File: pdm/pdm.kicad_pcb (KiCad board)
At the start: 2 copper layers, 169.5 x 69 mm, 100 parts, among them J1 Conn_01x05, J2 Conn_01x04_Male, Q1 Q_NPN_BCE, Q10 MMBT3904, Q2 Q_NPN_BCE, Q3 Q_NPN_BCE, Q4 Q_NPN_BCE, Q5 Q_NPN_BCE, Q6 MMBT3904, Q7 MMBT3904, Q8 MMBT3904, Q9 MMBT3904, SW1 SW_Push, U1 AZ1117CH-3_3TRG1, U10 BTS443P, U12 BTS443P, U2 SN65HVD233, U3 STM32F042G6Ux, U4 BTS443P, U6 BTS443P, U8 BTS443P

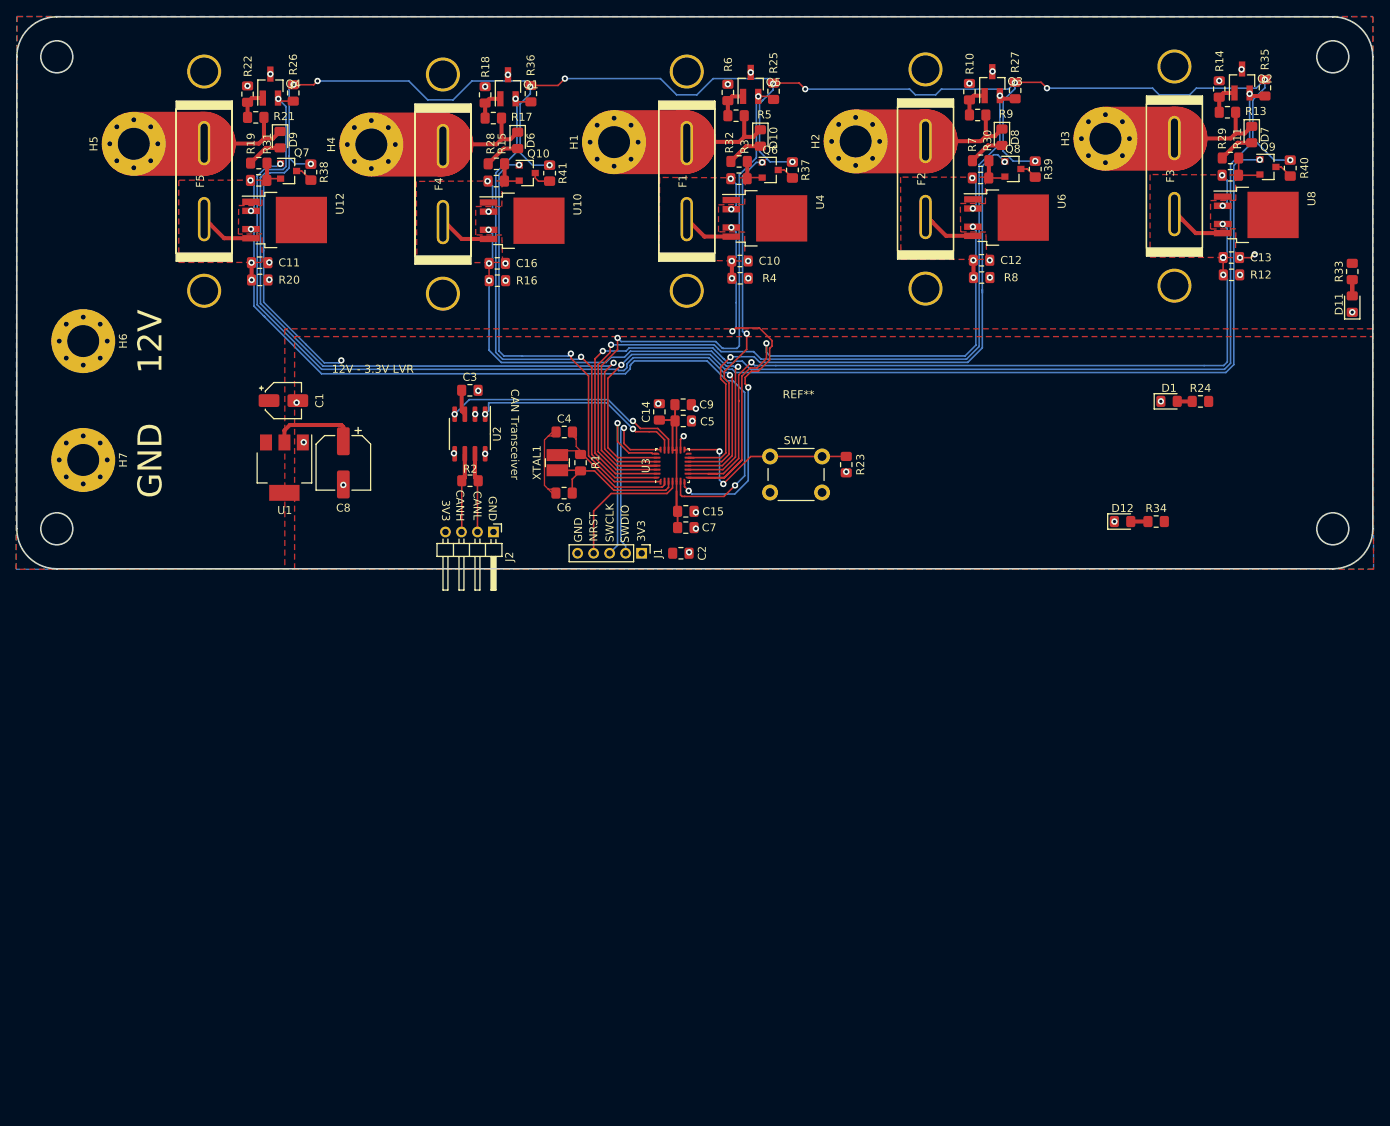
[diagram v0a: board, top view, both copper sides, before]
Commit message: changed to molex headers
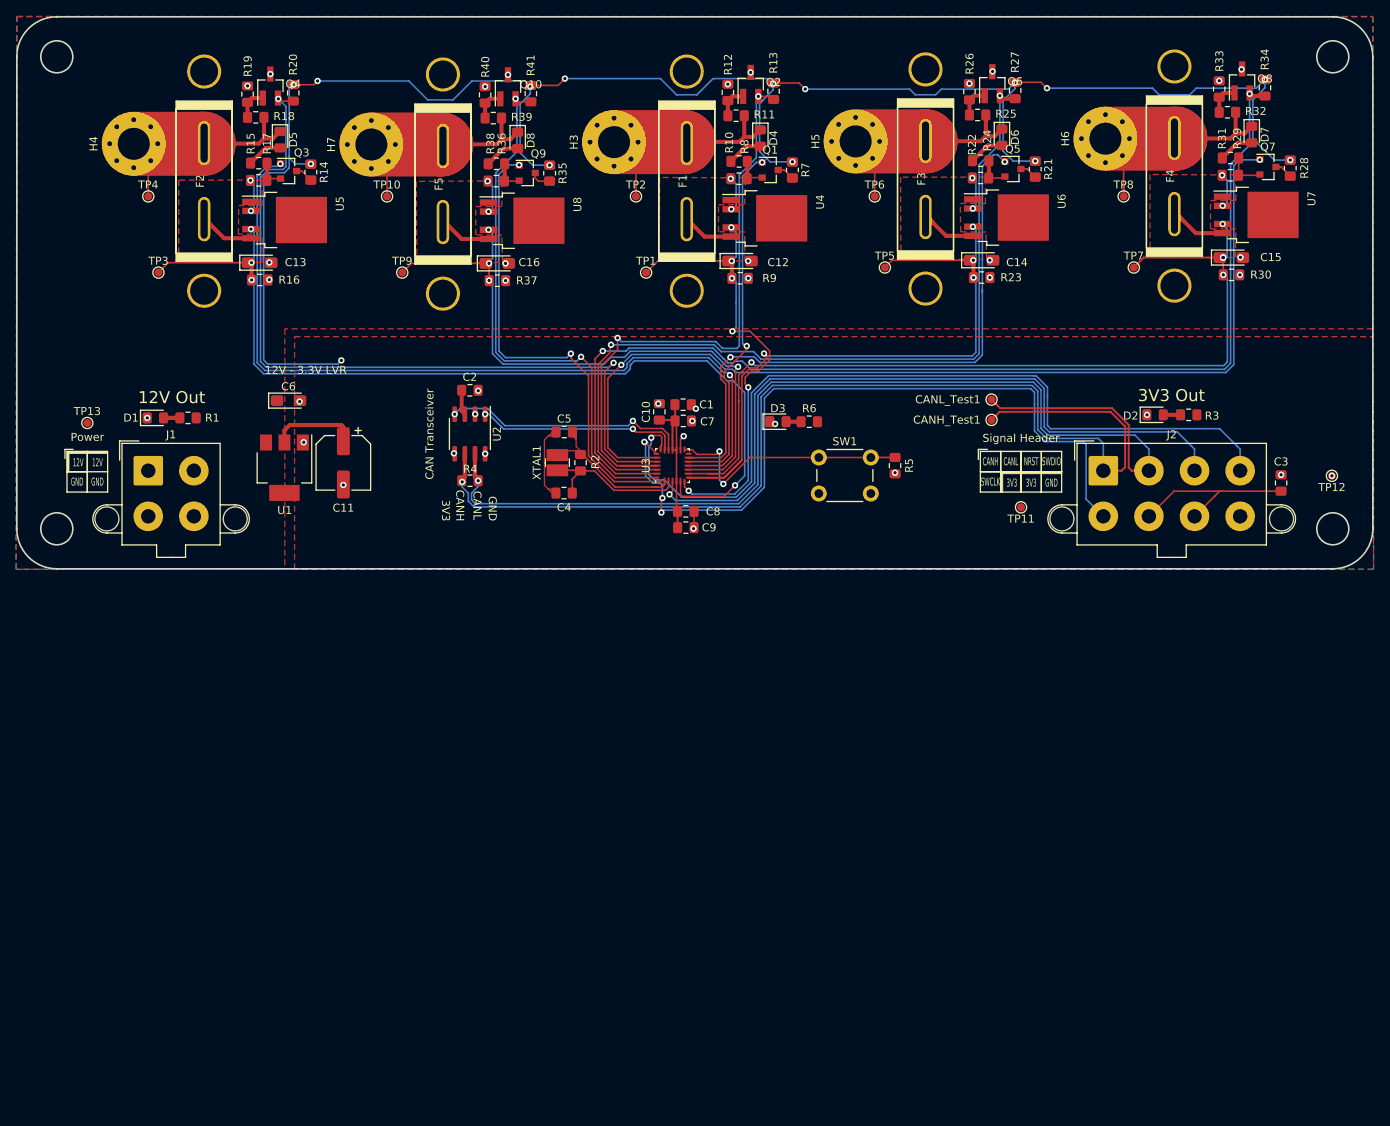
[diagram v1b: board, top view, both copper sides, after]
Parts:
- removed D11, D12: LED, LED_SMD:LED_0805_2012Metric_Pad1.15x1.40mm_HandSolder
- removed the H6 at (106.8, 62.5)
- removed the H7 at (106.8, 77.4)
- removed the R33 at (265.4, 53.8)
- removed the R34 at (240.9, 85.1)
- removed REF**: Panelized Blade Fuse Holder, Panelized Blade Fuse Holder
- added CANH_Test1: CANH_TEST, TestPoint:TestPoint_Pad_D1.0mm, F.Cu at (220.3, 72.4)
- added CANL_Test1: CANL_TEST, TestPoint:TestPoint_Pad_D1.0mm, F.Cu at (220.3, 69.8)
- added D1: LED, LED_SMD:LED_0805_2012Metric_Pad1.15x1.40mm_HandSolder, F.Cu at (115.8, 72.1)
- added D2: LED, LED_SMD:LED_0805_2012Metric_Pad1.15x1.40mm_HandSolder, F.Cu at (240.8, 71.8)
- added R1: 600R, Resistor_SMD:R_0805_2012Metric_Pad1.15x1.40mm_HandSolder, F.Cu at (119.9, 72.1)
- added R3: 600R, Resistor_SMD:R_0805_2012Metric_Pad1.15x1.40mm_HandSolder, F.Cu at (245.0, 71.8)
- added TP1: TestPoint_Probe, TestPoint:TestPoint_Pad_D1.0mm, F.Cu at (177.2, 54.0)
- added TP10: TestPoint_Probe, TestPoint:TestPoint_Pad_D1.0mm, F.Cu at (144.8, 44.5)
- added TP11: TestPoint_Probe, TestPoint:TestPoint_Pad_D1.0mm, F.Cu at (224.0, 83.3)
- added TP12: TestPoint_Probe, TestPoint:TestPoint_Pad_D1.0mm, F.Cu at (262.9, 79.4)
- added TP13: TestPoint_Probe, TestPoint:TestPoint_Pad_D1.0mm, F.Cu at (107.3, 72.8)
- added TP2: TestPoint_Probe, TestPoint:TestPoint_Pad_D1.0mm, F.Cu at (175.9, 44.5)
- added TP3: TestPoint_Probe, TestPoint:TestPoint_Pad_D1.0mm, F.Cu at (116.2, 54.0)
- added TP4: TestPoint_Probe, TestPoint:TestPoint_Pad_D1.0mm, F.Cu at (114.9, 44.5)
- added TP5: TestPoint_Probe, TestPoint:TestPoint_Pad_D1.0mm, F.Cu at (207.0, 53.3)
- added TP6: TestPoint_Probe, TestPoint:TestPoint_Pad_D1.0mm, F.Cu at (205.7, 44.5)
- added TP7: TestPoint_Probe, TestPoint:TestPoint_Pad_D1.0mm, F.Cu at (238.1, 53.3)
- added TP8: TestPoint_Probe, TestPoint:TestPoint_Pad_D1.0mm, F.Cu at (236.9, 44.5)
- added TP9: TestPoint_Probe, TestPoint:TestPoint_Pad_D1.0mm, F.Cu at (146.7, 54.0)
- C1: renamed from C9; value 100nF -> 0.1uF
- C12: renamed from C10; value 7.2uF -> 10uF; footprint Capacitor_SMD:C_0805_2012Metric_Pad1.15x1.40mm_HandSolder -> Capacitor_Tantalum_SMD:CP_EIA-3216-18_Kemet-A_Pad1.58x1.35mm_HandSolder
- C13: renamed from C11; value 7.2uF -> 10uF; footprint Capacitor_SMD:C_0805_2012Metric_Pad1.15x1.40mm_HandSolder -> Capacitor_Tantalum_SMD:CP_EIA-3216-18_Kemet-A_Pad1.58x1.35mm_HandSolder
- C14: renamed from C12; value 7.2uF -> 10uF; footprint Capacitor_SMD:C_0805_2012Metric_Pad1.15x1.40mm_HandSolder -> Capacitor_Tantalum_SMD:CP_EIA-3216-18_Kemet-A_Pad1.58x1.35mm_HandSolder
- C15: renamed from C13; value 7.2uF -> 10uF; footprint Capacitor_SMD:C_0805_2012Metric_Pad1.15x1.40mm_HandSolder -> Capacitor_Tantalum_SMD:CP_EIA-3216-18_Kemet-A_Pad1.58x1.35mm_HandSolder
- C16: value 7.2uF -> 10uF; footprint Capacitor_SMD:C_0805_2012Metric_Pad1.15x1.40mm_HandSolder -> Capacitor_Tantalum_SMD:CP_EIA-3216-18_Kemet-A_Pad1.58x1.35mm_HandSolder
- C2: renamed from C3; value 0.1 uF -> 0.1uF
- C3: renamed from C2; value 0.1 uF -> 0.1uF
- C4: renamed from C6; value 20p -> 20pF
- C5: renamed from C4; value 20p -> 20pF
- C6: renamed from C1; footprint Capacitor_SMD:CP_Elec_4x5.4 -> Capacitor_Tantalum_SMD:CP_EIA-3216-18_Kemet-A_Pad1.58x1.35mm_HandSolder
- C7: renamed from C5; value 100nF -> 0.1uF
- C9: renamed from C7; value 100nF -> 0.1uF
- J1: value Conn_01x05 -> Conn_01x04_Male; footprint Connector_PinHeader_2.00mm:PinHeader_1x05_P2.00mm_Vertical -> Connector_Molex:Molex_Mega-Fit_76829-0004_2x02_P5.70mm_Vertical
- J2: value Conn_01x04_Male -> Conn_01x08_Male; footprint Connector_PinHeader_2.00mm:PinHeader_1x04_P2.00mm_Horizontal -> Connector_Molex:Molex_Mega-Fit_76829-0008_2x04_P5.70mm_Vertical
- moved J2 76.6 mm to (234.3, 78.7), turned to 0 degrees
- moved C3 75.5 mm to (256.5, 80.3), turned to 90 degrees
- moved J1 62.5 mm to (114.9, 78.7), turned to 0 degrees
- moved D3 49.0 mm to (193.6, 72.6)
- moved R6 49.0 mm to (197.6, 72.6)
- moved R5 6.10 mm to (208.3, 78.1)
- moved SW1 6.10 mm to (198.8, 77.1)
- moved C6 0.64 mm to (132.5, 70.0)
- renumbered C14 to C10, C8 to C11, C15 to C8, D1 to D3, D10 to D4, D9 to D5, D8 to D6, D6 to D8, F5 to F2, F2 to F3, F3 to F4, F4 to F5, H1 to H3, H5 to H4, H2 to H5, H3 to H6, H4 to H7, Q6 to Q1, Q1 to Q10, Q5 to Q2, Q7 to Q3, Q8 to Q5, Q3 to Q6, Q9 to Q7, Q2 to Q8, Q10 to Q9, R32 to R10, R5 to R11, R6 to R12, R25 to R13, R38 to R14, R19 to R15, R20 to R16, R31 to R17, R21 to R18, R22 to R19, R1 to R2, R26 to R20, R39 to R21, R7 to R22, R8 to R23, R30 to R24, R9 to R25, R10 to R26, R40 to R28, R11 to R29, R12 to R30, R29 to R31, R13 to R32, R14 to R33, R35 to R34, R41 to R35, R15 to R36, R16 to R37, R28 to R38, R17 to R39, R2 to R4, R18 to R40, R36 to R41, R23 to R5, R24 to R6, R37 to R7, R3 to R8, R4 to R9, U12 to U5, U8 to U7, U10 to U8
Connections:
- J1 pad 1: +3V3 -> +12V
- J1 pad 2: /SWDIO -> +12V
- J1 pad 3: /SWCLK -> GND
- J1 pad 4: /NRST -> GND
- J2 pad 1: GND -> /_P
- J2 pad 3: /_P -> /NRST
- J2 pad 4: +3V3 -> /SWDIO
- R6 pad 2: /DEBUG_LED -> (no net)
- U1 pad 4: Net-(U1-Pad4) -> (no net)
- U3 pad 14: /LED_DEBUG -> (no net)
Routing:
- net /_N: track 10.0 -> 138.9 mm, vias 0 -> 1
- net /_P: track 10.3 -> 133.5 mm, vias 0 -> 1
- net /SWDIO: track 23.4 -> 105.2 mm
- net /NRST: track 17.2 -> 89.7 mm, vias 0 -> 1
- net /SWCLK: track 24.5 -> 94.6 mm, vias 1 -> 3
- net +3V3: track 268.4 -> 292.4 mm
- net /sense1: track 98.9 -> 115.2 mm
- net /sense4: track 99.7 -> 111.0 mm
- net /sense5: track 66.6 -> 77.7 mm
- net /sense3: track 75.2 -> 84.7 mm
- net /sense2: track 49.1 -> 58.5 mm
- net /sheet5F95602F/vload: track 21.6 -> 30.5 mm
- net /sheet5F955EDF/vload: track 21.6 -> 29.6 mm
- net /sheet5F955F69/vload: track 21.6 -> 29.6 mm
- net /fuse_block/vload: track 21.6 -> 28.9 mm
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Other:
- board text added: "12V Out"
- board text added: "3V3 Out"
- board text added: "Power"
- board text added: "Signal Header"

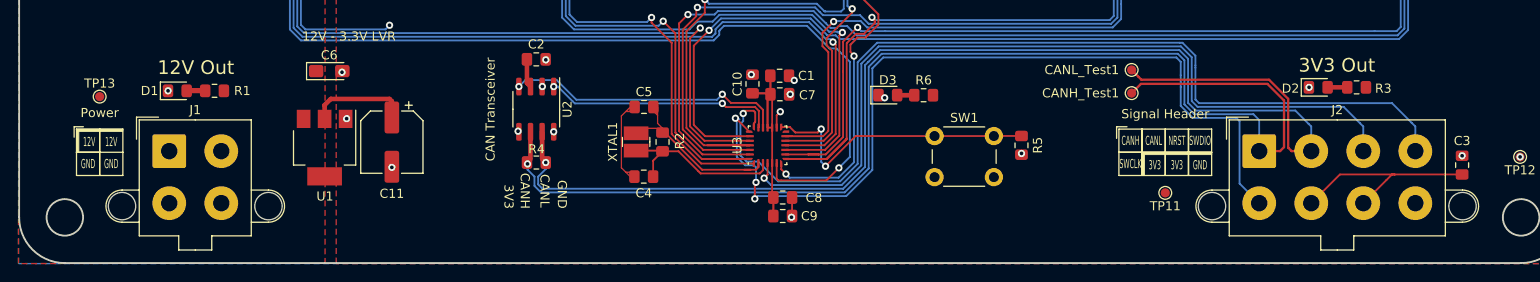
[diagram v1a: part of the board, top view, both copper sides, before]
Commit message: rotated molex
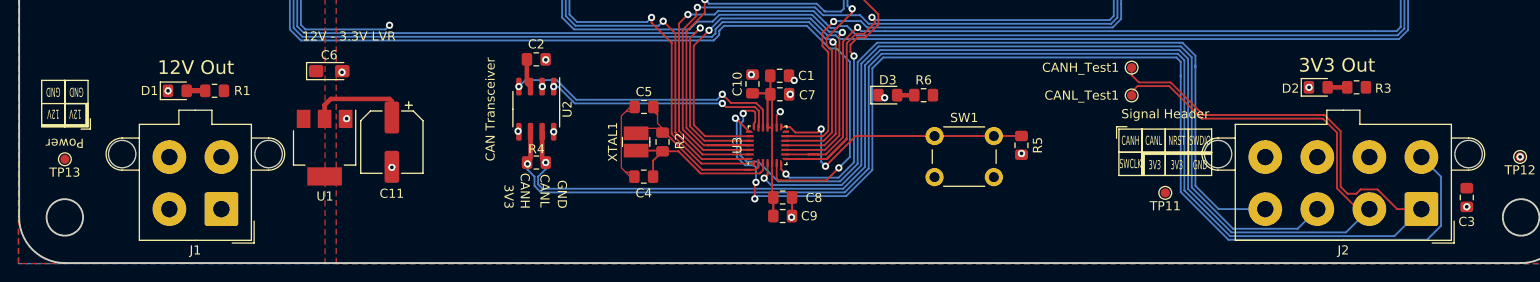
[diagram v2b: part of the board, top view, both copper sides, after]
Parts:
- moved J2 18.9 mm to (252.1, 85.1), turned to 180 degrees
- moved J1 8.54 mm to (120.7, 85.1), turned to 180 degrees
- moved TP13 7.85 mm to (103.5, 79.6), turned to 180 degrees
- moved C3 3.58 mm to (257.0, 83.8), turned to 270 degrees
- moved CANL_Test1 2.79 mm to (220.3, 72.6)
- moved CANH_Test1 2.79 mm to (220.3, 69.6)
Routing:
- net /_P: track 133.5 -> 176.6 mm
- net /SWCLK: track 94.6 -> 127.0 mm
- net /_N: track 138.9 -> 163.3 mm
- net +3V3: track 292.4 -> 270.4 mm
- net /SWDIO: track 105.2 -> 95.6 mm
- net /NRST: track 89.7 -> 93.0 mm
